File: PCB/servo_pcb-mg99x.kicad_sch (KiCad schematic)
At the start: 31 parts, among them M1 M1, M2 M2, M3 M2, M4 M2, M5 M2, U1 MM32G0001, U2 SL7533-3, U3 CP2119L, U4 INA180A2, U5 AS5600

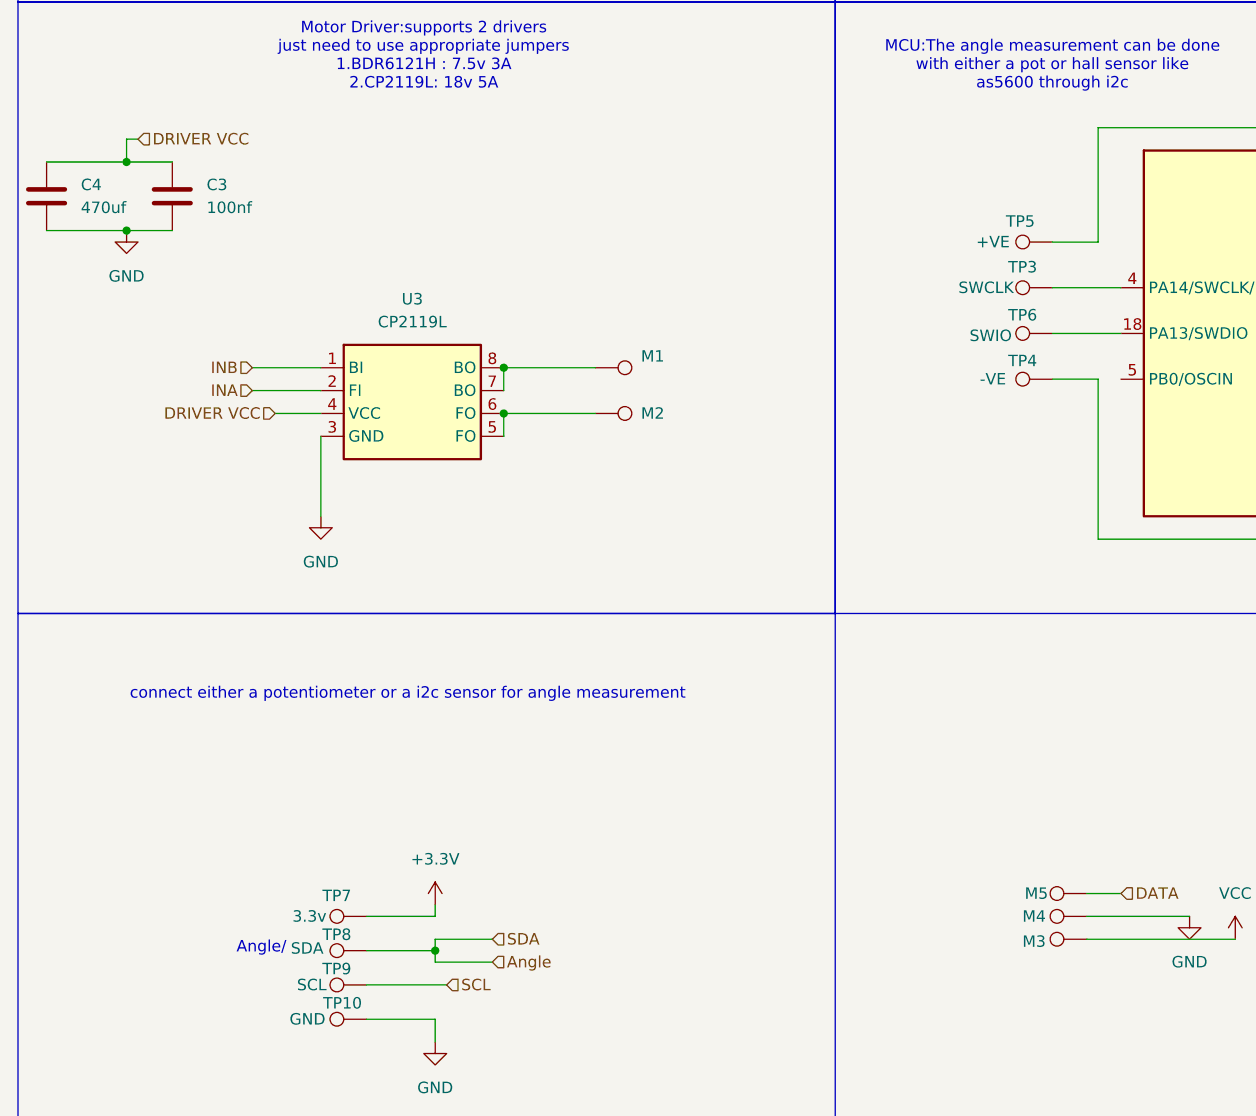
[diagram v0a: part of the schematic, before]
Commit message: updated  the pcb for generic motors
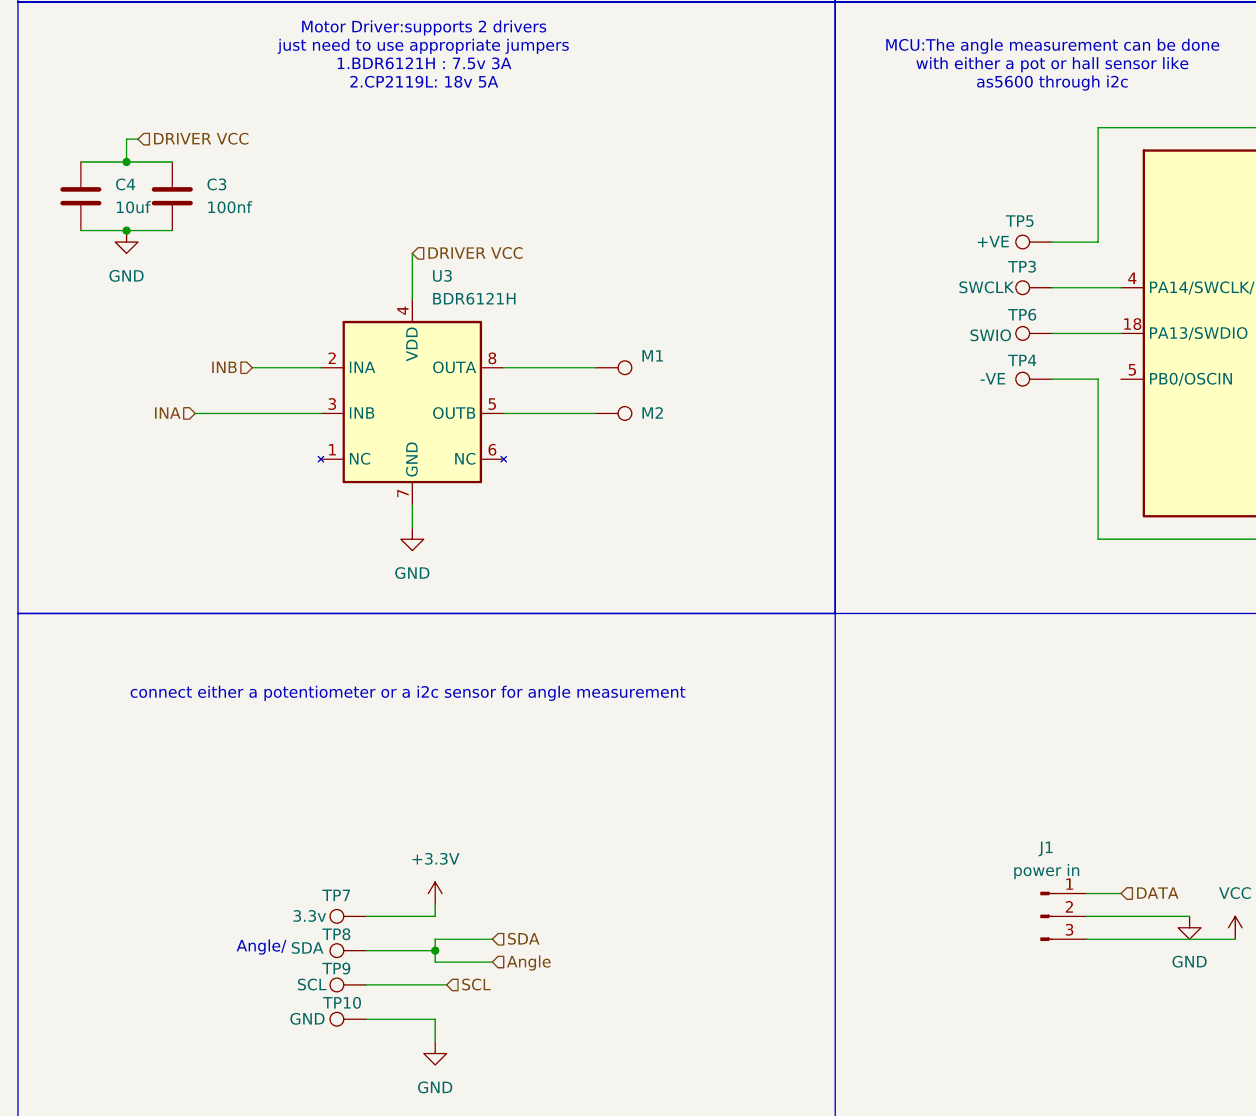
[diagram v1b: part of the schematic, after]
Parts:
- removed M3, M4, M5: M2, TestPoint:TestPoint_THTPad_3.0x3.0mm_Drill1.5mm, symbol Connector:TestPoint
- removed U3: CP2119L, Package_SO:SOIC-8_3.9x4.9mm_P1.27mm, symbol CP2119L:CP2119L
- added J1: power in, Connector_PinHeader_2.54mm:PinHeader_1x03_P2.54mm_Vertical, symbol Connector:Conn_01x03_Pin
- added U3: BDR6121H, Package_SO:SOIC-8_3.9x4.9mm_P1.27mm, symbol BDR6121H:BDR6121H
- C4: value 470uf -> 10uf; footprint Capacitor_THT:CP_Radial_D8.0mm_P5.00mm -> Capacitor_SMD:C_0805_2012Metric_Pad1.18x1.45mm_HandSolder
- M1, M2: footprint TestPoint:TestPoint_THTPad_3.0x3.0mm_Drill1.5mm -> TestPoint:TestPoint_Pad_2.5x2.5mm
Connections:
- net DATA: now also J1.1 (Pin_1)
- net DRIVER VCC: now also U3.4 (VDD)
- net GND: now also J1.2 (Pin_2), U3.7 (GND)
- net INA: now also U3.3 (INB)
- net INB: now also U3.2 (INA)
- net VCC: now also J1.3 (Pin_3)
- net at M1.1: now also U3.8 (OUTA)
- net at M2.1: now also U3.5 (OUTB)
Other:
- moved on the sheet: C4

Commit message: updated docs
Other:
- note added: "Motor Driver: BDR6121H : 7.5v 1.5A"
- note removed: "Motor Driver:supports 2 drivers just need to use appropriate jumpers 1.BDR6121H : 7.5v 3A 2.CP2119L: 18v 5A"
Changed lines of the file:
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@@
 		)
 	)
-	(text "Motor Driver:supports 2 drivers\njust need to use appropriate jumpers\n1.BDR6121H : 7.5v 3A\n2.CP2119L: 18v 5A \n"
+	(text "Motor Driver: BDR6121H : 7.5v 1.5A\n\n"
 		(exclude_from_sim no)
 		(at 57.15 73.406 0)
